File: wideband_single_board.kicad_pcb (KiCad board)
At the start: 2 copper layers, 38.5 x 48 mm, 79 parts, among them J1 Conn_02x06_Top_Bottom, J2 USB_B_Micro, J3 FTSH-107-01-F-DV-K, Q1 BTS3028, SW1 SW_Push, U1 XC6206P332MR, U2 MCP6004, U3 LM78M05_TO252, U4 AD8628, U5 TJA1051T-3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

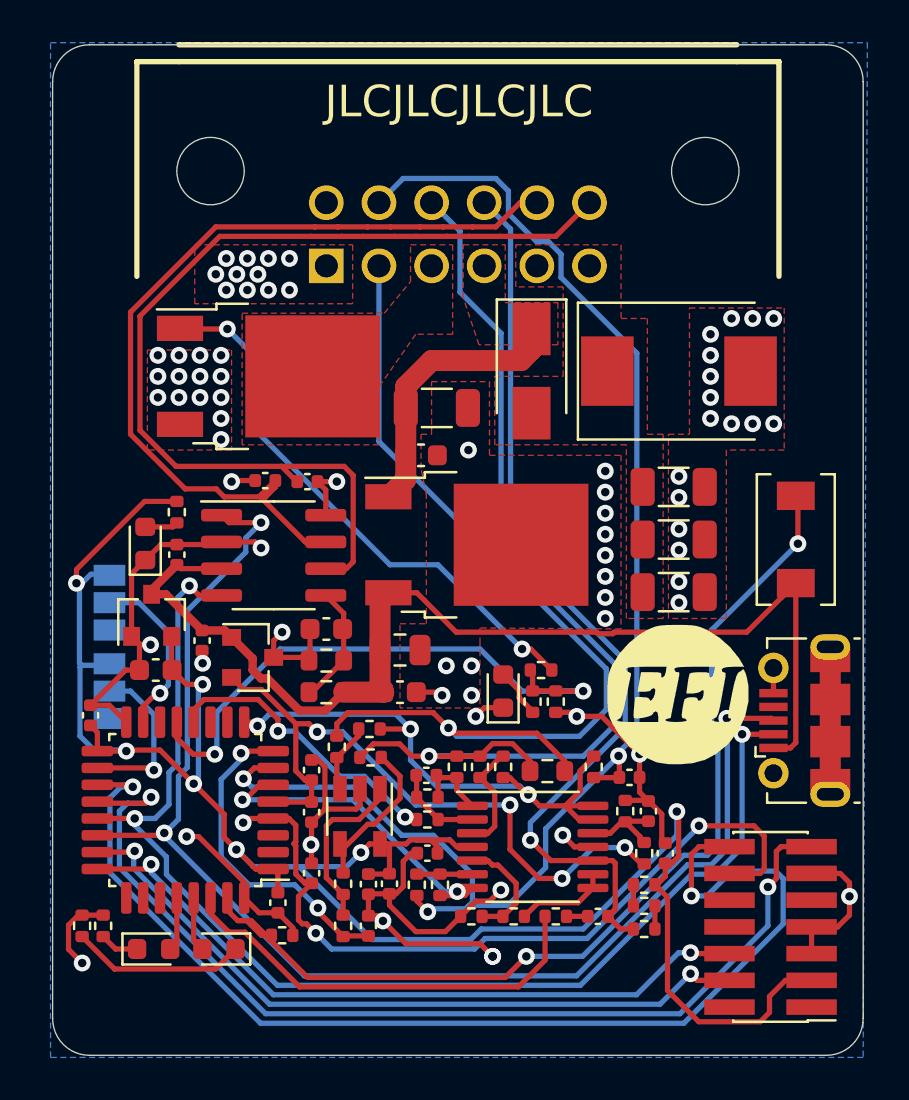
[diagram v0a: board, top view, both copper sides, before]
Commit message: changed overall layout of the board and made a connector board to wire up two LSU4.9 to 2 board in a single case
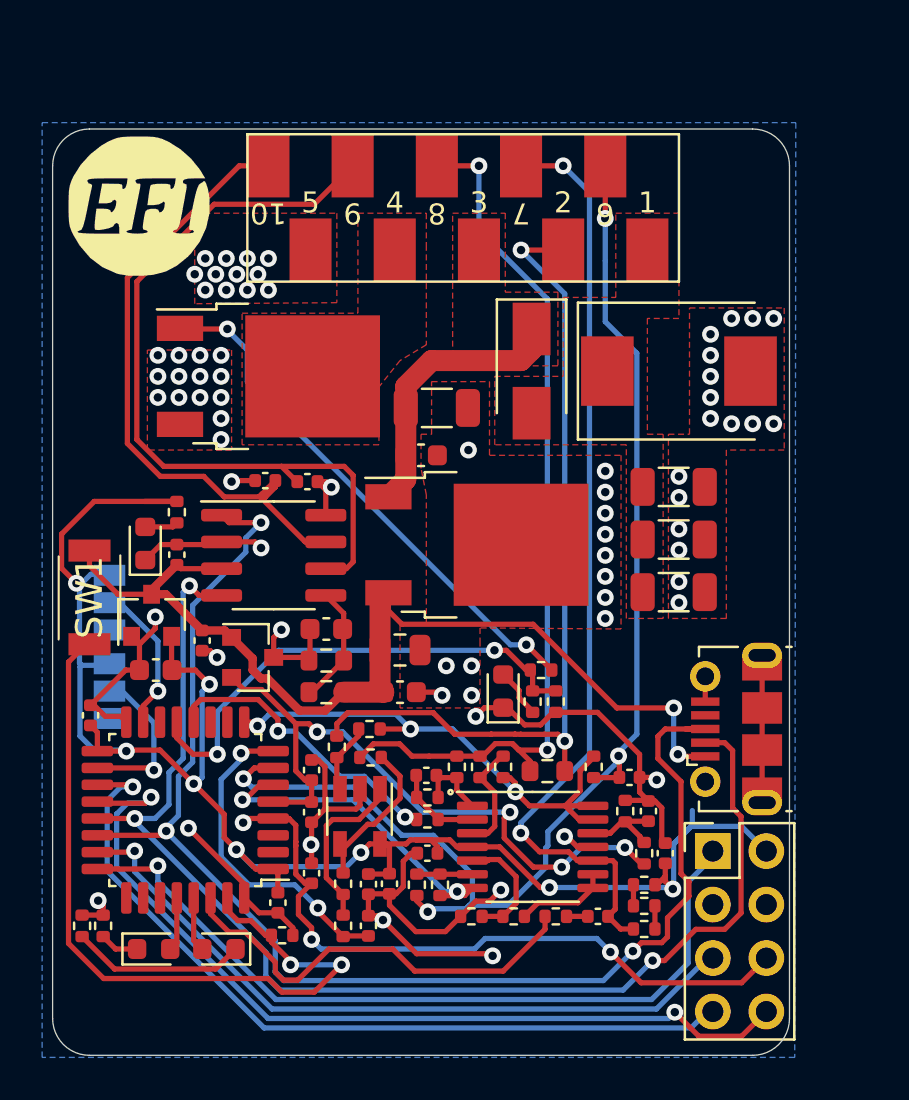
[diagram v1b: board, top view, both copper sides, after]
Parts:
- removed the G? at (145.2, 89.4)
- added G?: LOGO, lib_wideband_sigle_board:LOGO, F.Cu at (119.6, 66.2)
- J1: value Conn_02x06_Top_Bottom -> Conn_02x05_Top_Bottom; footprint Lib_wideband_2.0:JAE_MX23A12NF1 -> TestPoint:Solder_pad_5X2X3.0X2.0mm
- J3: value FTSH-107-01-F-DV-K -> Conn_02x04_Top_Bottom; footprint Connector_PinHeader_1.27mm:PinHeader_2x07_P1.27mm_Vertical_SMD -> Connector_PinHeader_2.54mm:PinHeader_2x04_P2.54mm_Vertical
- SW1: footprint Lib_wideband_2.0:TS-1088 -> lib_wideband_sigle_board:TS1088R02026
- moved SW1 33.7 mm to (117.2, 84.8), turned to 90 degrees
- moved J3 4.52 mm to (146.9, 96.8), turned to 0 degrees
- moved J2 3.26 mm to (148.0, 91.0)
- moved J1 1.75 mm to (134.8, 66.2), turned to 0 degrees
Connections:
- J1 pad 1: GND -> 12V_RAW
- J1 pad 10: /LSU_Un -> /CAN_H
- J1 pad 3: /LSU_Heater- -> /LSU_Heater+
- J1 pad 4: /LSU_Heater+ -> /LSU_Heater-
- J1 pad 5: 12V_RAW -> GND
- J1 pad 6: 12V_RAW -> /LSU_Vm
- J1 pad 7: Net-(J1-Pad7) -> /LSU_Un
- J1 pad 8: /LSU_Vm -> /LSU_Rtrim
- J1 pad 9: /LSU_Rtrim -> /CAN_L
- J3 pad 1: Net-(J3-Pad1) -> /SWCLK
- J3 pad 2: Net-(J3-Pad2) -> +3V3
- J3 pad 3: +3V3 -> GND
- J3 pad 4: /SWDIO -> GND
- J3 pad 5: GND -> /SWDIO
- J3 pad 6: /SWCLK -> /nRESET
- J3 pad 7: GND -> /UART_TX
- J3 pad 8: Net-(J3-Pad8) -> /UART_RX
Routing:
- net +3V3: track 99.9 -> 82.7 mm, vias 7 -> 8
- net /UART_TX: track 54.6 -> 38.5 mm, vias 2 -> 1
- net /Boot0: track 49.4 -> 37.1 mm
- net /CAN_H: track 41.0 -> 30.5 mm
- net /CAN_L: track 46.6 -> 37.6 mm
- net /LSU_Vm: track 69.8 -> 61.9 mm, vias 3 -> 4
- net /LSU_Ip: track 46.8 -> 39.8 mm, vias 1 -> 2
- net GND: track 93.6 -> 86.8 mm, vias 73 -> 71
- net +5V: track 53.9 -> 47.4 mm, vias 0 -> 2
- net /UART_RX: track 48.0 -> 42.1 mm
- net /LSU_Rtrim: track 47.5 -> 42.5 mm, vias 1 -> 2
- net /heater_pwm: track 27.8 -> 23.6 mm
- net /nRESET: track 36.7 -> 32.5 mm
- net /SWCLK: track 33.8 -> 37.7 mm, vias 2 -> 1
- net /CAN_TX: track 62.7 -> 64.7 mm
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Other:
- board size 38.5 x 48 mm -> 35 x 44 mm
- board text added: "1"
- board text added: "1 12Vin 2 Ip 3 Uh+ 4 Uh- 5 GND 6 Vm 7 Un 8 IA 9 CAN L 10 CAN H"
- board text added: "10"
- board text added: "2"
- board text added: "3"
- board text added: "4"
- board text added: "5"
- board text added: "6"
- board text added: "7"
- board text added: "8"
- board text added: "9"
- board text removed: "JLCJLCJLCJLC"
